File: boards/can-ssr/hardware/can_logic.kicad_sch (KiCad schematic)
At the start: 31 parts, among them J1 CAN IN, J2 CAN OUT, J3 ICSP, J4 UART, SW1 ADDR, U1 R-78E5.0-1.0, U2 MCP2562FD-E/P, U3 PIC18F47Q84-I/P, Y1 16MHz

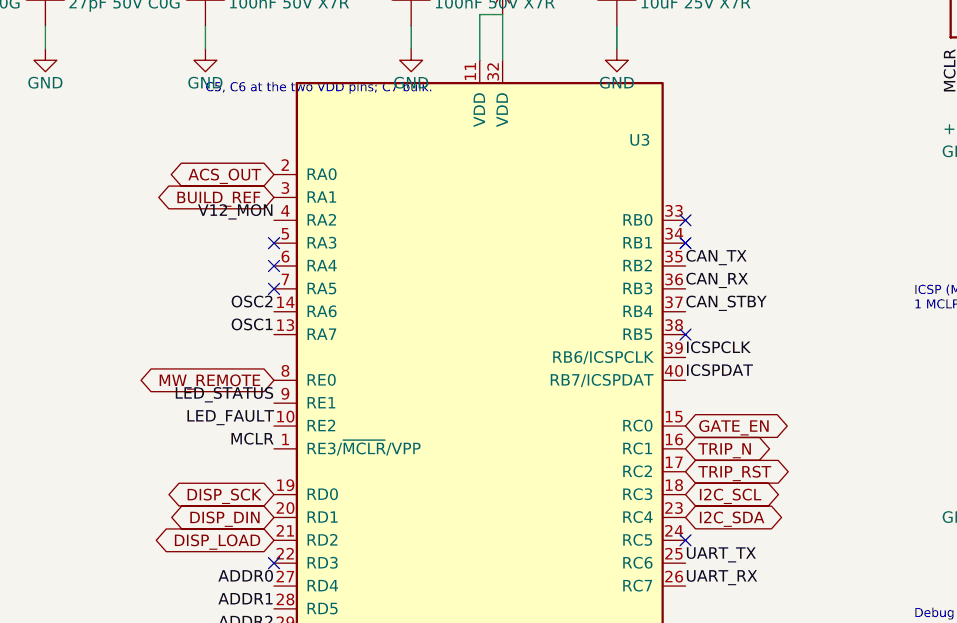
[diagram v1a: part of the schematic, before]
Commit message: can-ssr schematic: overcurrent trip and gate-drive block
- Build resistor R20 (HC 7.15k / STD 16.2k / HV 35.7k) over 10k sets the
  trip threshold Vth (60 / 35 / 15 A on the ACS770-100U) and is read by
  the PIC as BUILD_REF; open R20 = always tripped
- LM393B comparator on the filtered ACS770 output, latched by a BAT54
  that drags Vth below the 0.5 V zero-current level; TRIP_RST (2N7002)
  releases it
- VOM1271 LED string driven ~21 mA through two series 2N7002s:
  GATE_EN AND TRIP_OK, so firmware cannot override a hardware trip
- ACS770 ADC filter; PIC nets renamed ACS_ADC and TRIP_OK

Co-Authored-By: Claude Opus 5.5 <noreply@anthropic.com>
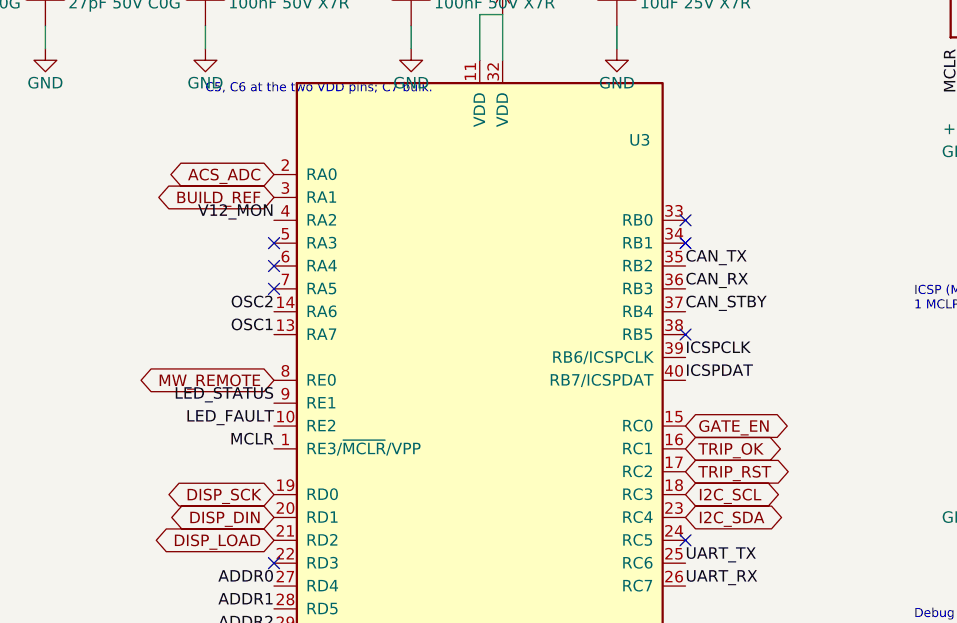
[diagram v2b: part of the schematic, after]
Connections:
- net ACS_OUT renamed ACS_ADC
- net TRIP_N renamed TRIP_OK

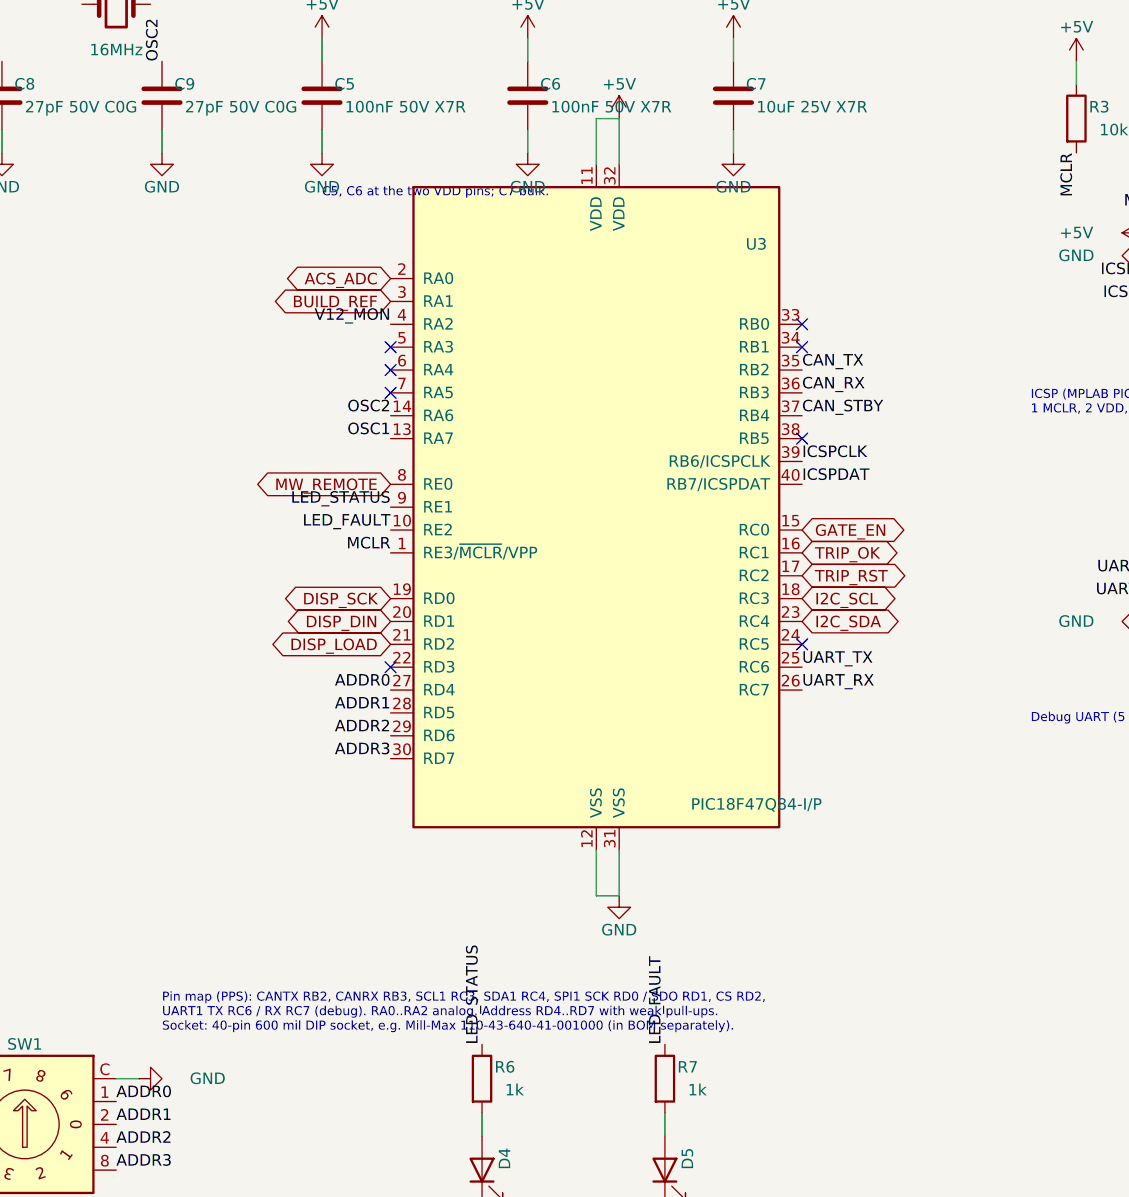
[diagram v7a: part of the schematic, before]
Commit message: can-ssr: PIC in TQFP-44, barrier moved up, re-placed
- Thl_MCU:PIC18F47Q84-IPT (TQFP-44) symbol from DS40002213C Table 3-2;
  U3 switched from the PDIP-40; schematic regenerated (pins verified)
- sync_pcb.py swaps a footprint in place when the schematic changes it
- Barrier at y ~42-48; ADC cluster in the band under the ISO1640, DACs
  between the ACS770 and J30 (right edge); trip circuit and VOM LED drive
  on the bottom under the display. No courtyard or clearance errors.
- Docs: MCU is now PIC18F47Q84-I/PT

Co-Authored-By: Claude Opus 5.5 <noreply@anthropic.com>
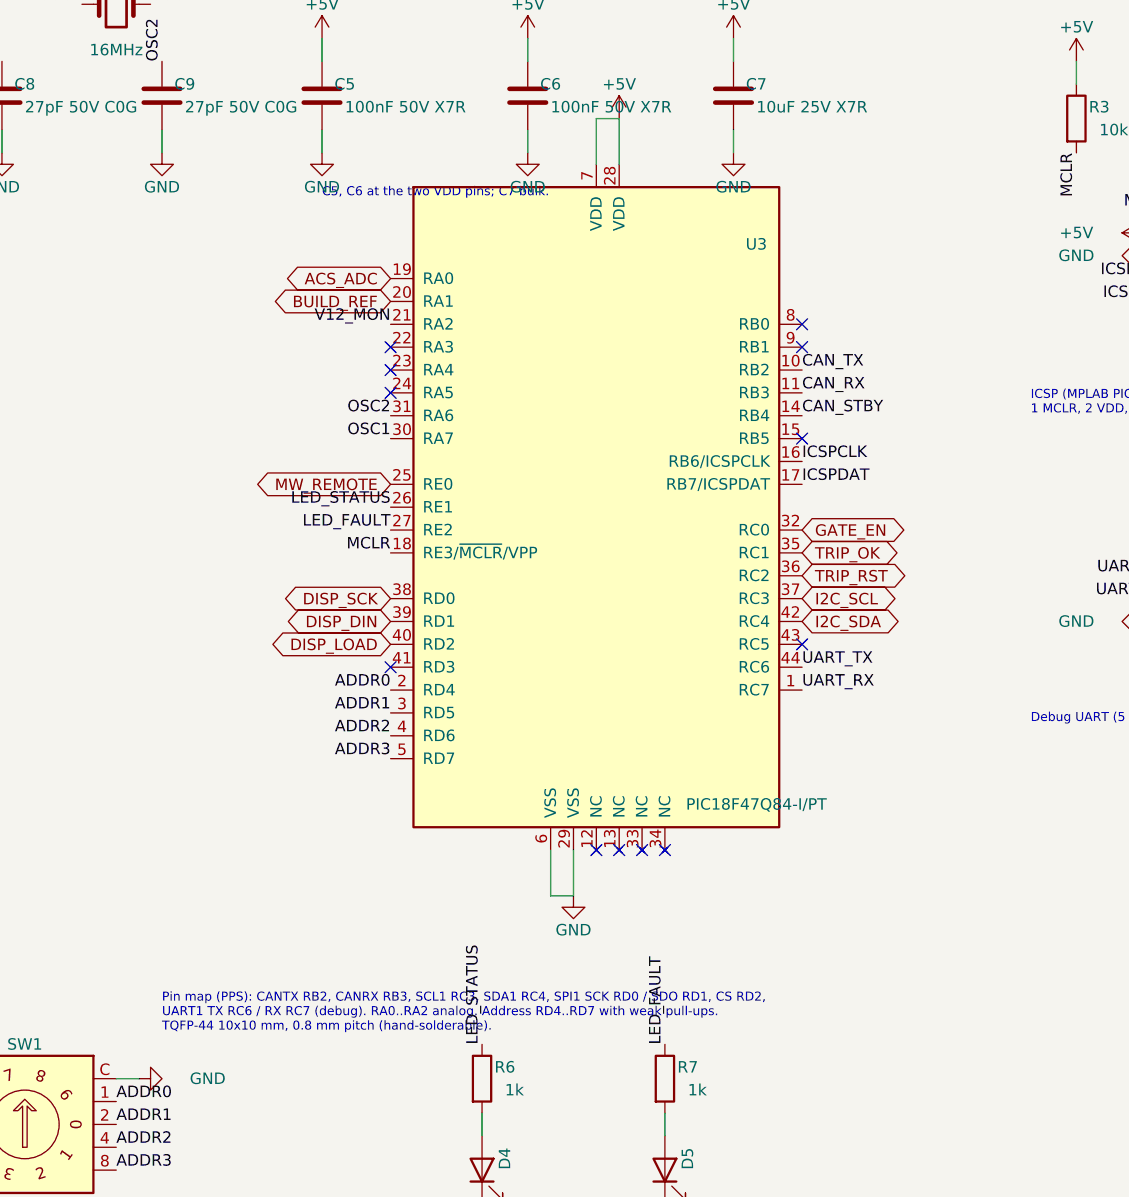
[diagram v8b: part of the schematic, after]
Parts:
- removed U3: PIC18F47Q84-I/P, Package_DIP:DIP-40_W15.24mm_Socket_LongPads, symbol Thl_MCU:PIC18F47Q84-IP
- added U3: PIC18F47Q84-I/PT, Package_QFP:TQFP-44_10x10mm_P0.8mm, symbol Thl_MCU:PIC18F47Q84-IPT
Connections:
- net +5V: now also U3.28 (VDD), U3.7 (VDD)
- net ACS_ADC: now also U3.19 (RA0)
- net ADDR0: now also U3.2 (RD4)
- net ADDR1: now also U3.3 (RD5)
- net ADDR2: now also U3.4 (RD6)
- net ADDR3: now also U3.5 (RD7)
- net BUILD_REF: now also U3.20 (RA1)
- net CAN_RX: now also U3.11 (RB3)
- net CAN_STBY: now also U3.14 (RB4)
- net CAN_TX: now also U3.10 (RB2)
- net DISP_DIN: now also U3.39 (RD1)
- net DISP_LOAD: now also U3.40 (RD2)
- net DISP_SCK: now also U3.38 (RD0)
- net GATE_EN: now also U3.32 (RC0)
- net GND: now also U3.29 (VSS), U3.6 (VSS)
- net I2C_SCL: now also U3.37 (RC3)
- net I2C_SDA: now also U3.42 (RC4)
- net ICSPCLK: now also U3.16 (RB6/ICSPCLK)
- net ICSPDAT: now also U3.17 (RB7/ICSPDAT)
- net LED_FAULT: now also U3.27 (RE2)
- net LED_STATUS: now also U3.26 (RE1)
- net MCLR: now also U3.18 (RE3/~{MCLR}/VPP)
- net MW_REMOTE: now also U3.25 (RE0)
- net OSC1: now also U3.30 (RA7)
- net OSC2: now also U3.31 (RA6)
- net TRIP_OK: now also U3.35 (RC1)
- net TRIP_RST: now also U3.36 (RC2)
- net UART_RX: now also U3.1 (RC7)
- net UART_TX: now also U3.44 (RC6)
- net V12_MON: now also U3.21 (RA2)
- no-connect marks 9 -> 13
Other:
- note added: "Pin map (PPS): CANTX RB2, CANRX RB3, SCL1 RC3, SDA1 RC4, SPI1 SCK RD0 / SDO RD1, CS RD2, UART1 TX RC6 / RX RC7 (debug). RA0..RA2 analog. Address RD4..RD7 with weak pull-ups. TQFP-44 10x10 mm, 0.8 mm pitch (hand-solderable)."
- note removed: "Pin map (PPS): CANTX RB2, CANRX RB3, SCL1 RC3, SDA1 RC4, SPI1 SCK RD0 / SDO RD1, CS RD2, UART1 TX RC6 / RX RC7 (debug). RA0..RA2 analog. Address RD4..RD7 with weak pull-ups. Socket: 40-pin 600 mil DIP socket, e.g. Mill-Max 110-43-640-41-001000 (in BOM separately)."
